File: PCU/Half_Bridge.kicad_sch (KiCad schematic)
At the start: 25 parts, among them IC7 LM321LVIDBVR, Q1 SQJA06EP-T1_GE3, Q2 SQJA06EP-T1_GE3, U1 INA181A1IDBVR

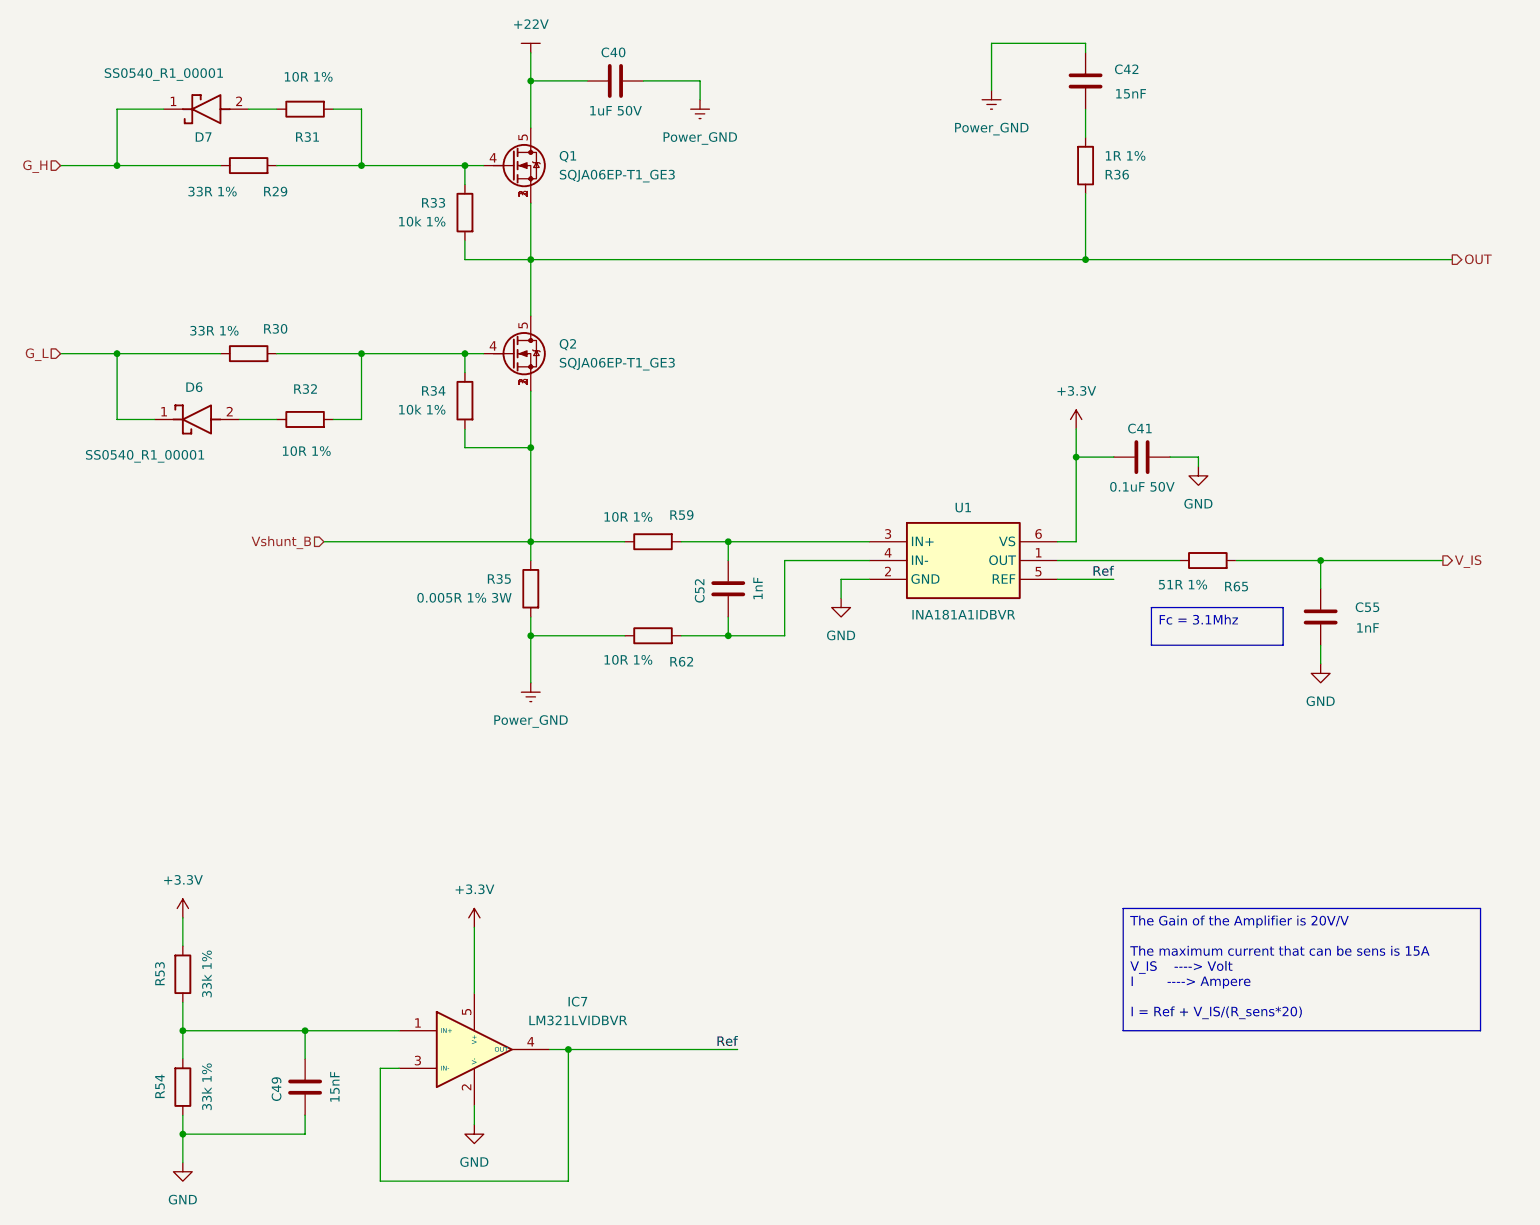
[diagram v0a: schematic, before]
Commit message: ESC Block Updated
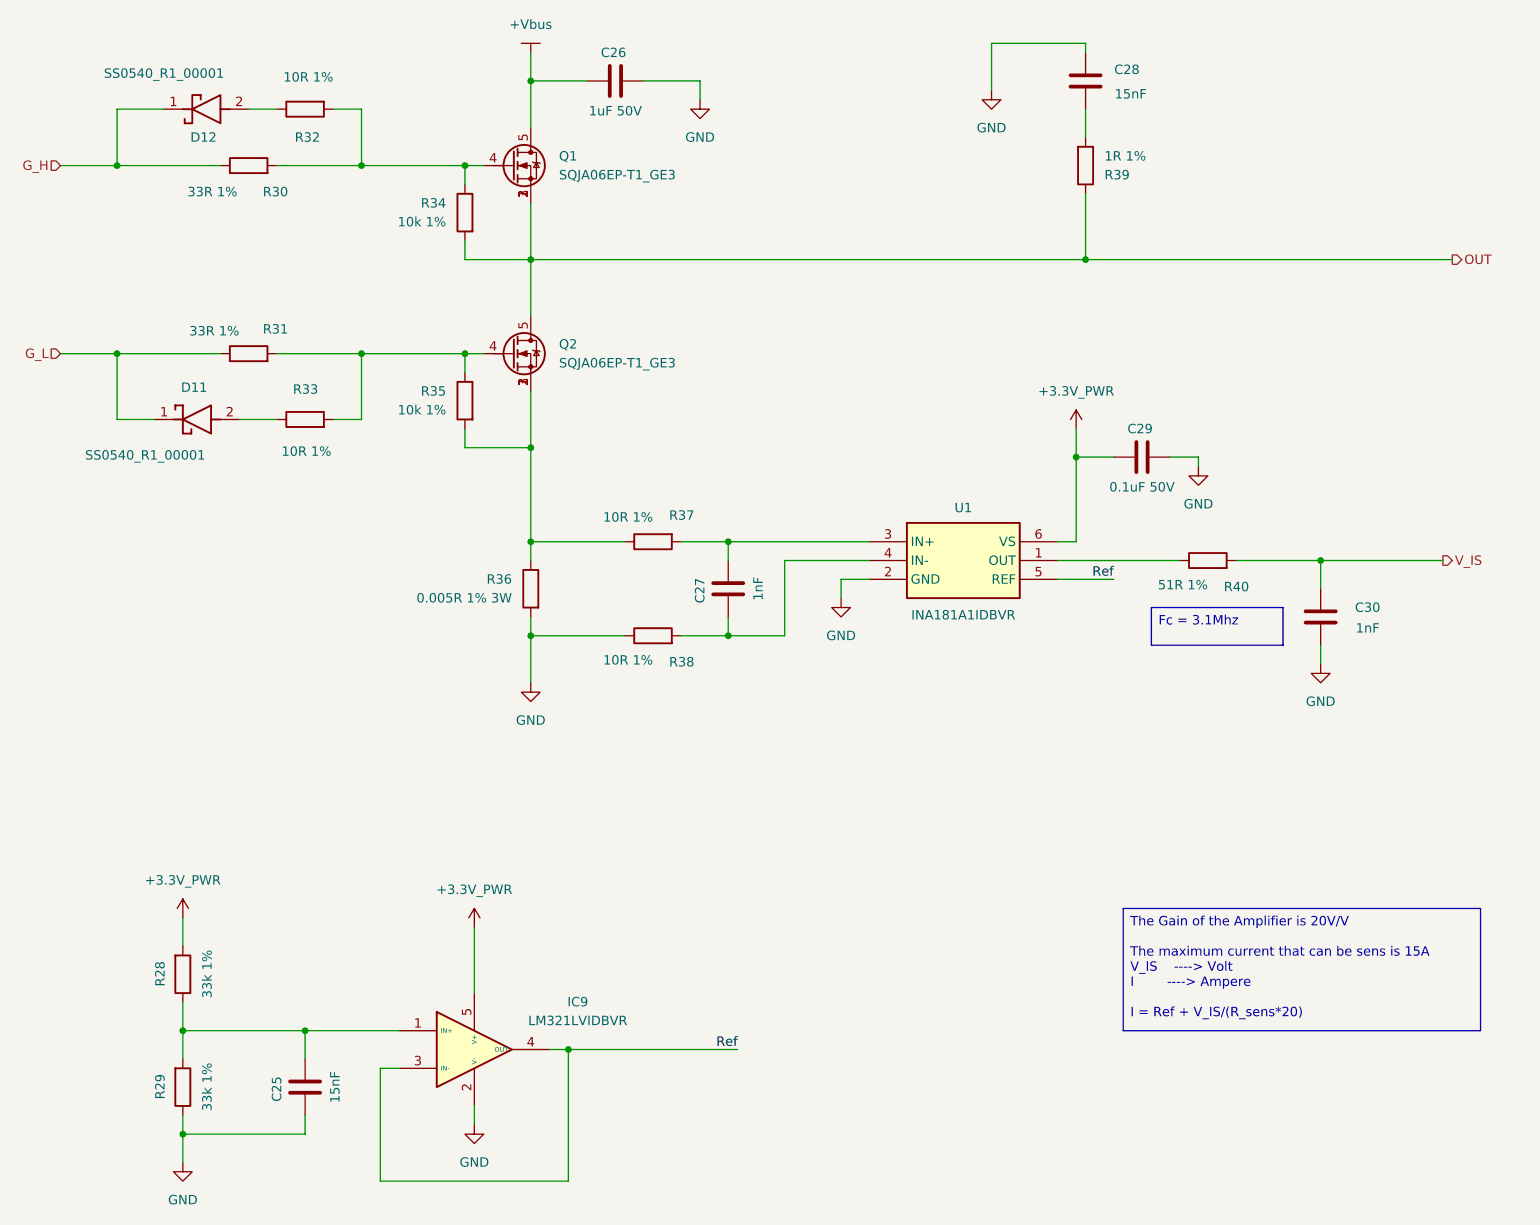
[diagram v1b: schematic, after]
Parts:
- IC9: renamed from IC7; footprint SOT95P280X145-5N -> BassingaLib_Op_Amp:SOT95P280X145-5N
- renumbered C49 to C25, C40 to C26, C52 to C27, C42 to C28, C41 to C29, C55 to C30, D6 to D11, D7 to D12, R53 to R28, R54 to R29, R29 to R30, R30 to R31, R31 to R32, R32 to R33, R33 to R34, R34 to R35, R35 to R36, R59 to R37, R62 to R38, R36 to R39, R65 to R40
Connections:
- net Power_GND is gone; now on net GND: C26.2, C28.1, R36.2, R38.1
- net +22V renamed +Vbus
- net +3.3V renamed +3.3V_PWR
- net Vshunt_B: no longer names the net of Q2.1, Q2.2, Q2.3, R35.2, R36.1, R37.1

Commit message: high power supply block
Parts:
- added C194: 0.1uF 50V, Capacitor_SMD:C_0603_1608Metric, symbol Device:C
- added C206: 1uF 50V, Capacitor_SMD:C_0805_2012Metric, symbol Device:C
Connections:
- net GND: now also C194.2, C206.2
- net +3.3V_PWR renamed +3.3V_Analog
- net +3.3V_Analog: now also C194.1, C206.1
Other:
- moved on the sheet: C29, C30, R40, U1

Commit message: Supervisor Block
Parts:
- renumbered C194 to C26, C26 to C27, C27 to C28, C28 to C29, C206 to C30, C29 to C31, C30 to C32, D11 to D12, D12 to D13

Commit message: PCB Design started
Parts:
- Q1, Q2: footprint Package_SO:PowerPAK_SO-8L_Single -> BassingaLib_Mosfets:SQJ402EPT1
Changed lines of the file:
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@@
 			)
 		)
-		(property "Footprint" "Package_SO:PowerPAK_SO-8L_Single"
+		(property "Footprint" "BassingaLib_Mosfets:SQJ402EPT1"
 			(at 88.646 65.532 0)
 			(effects
@@
 			)
 		)
-		(property "Footprint" "Package_SO:PowerPAK_SO-8L_Single"
+		(property "Footprint" "BassingaLib_Mosfets:SQJ402EPT1"
 			(at 88.646 90.932 0)
 			(effects

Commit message: Fly controller design started
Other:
- company: BASSINGA Lab -> BASSINGA_LAB
- title: ESC -> Propulsion Control Unit
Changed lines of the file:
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@@
 	(paper "A4")
 	(title_block
-		(title "ESC")
+		(title "Propulsion Control Unit")
 		(date "2025-05-21")
 		(rev "v1.0")
-		(company "BASSINGA Lab")
+		(company "BASSINGA_LAB")
+		(comment 1 "Copyright © 2025 Andresse Brisel BASSINGA ")
 	)
 	(text_box "Fc = 3.1Mhz"
